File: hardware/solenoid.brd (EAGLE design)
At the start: 37.3 x 34 mm, 32 parts, among them U2 AP2204R

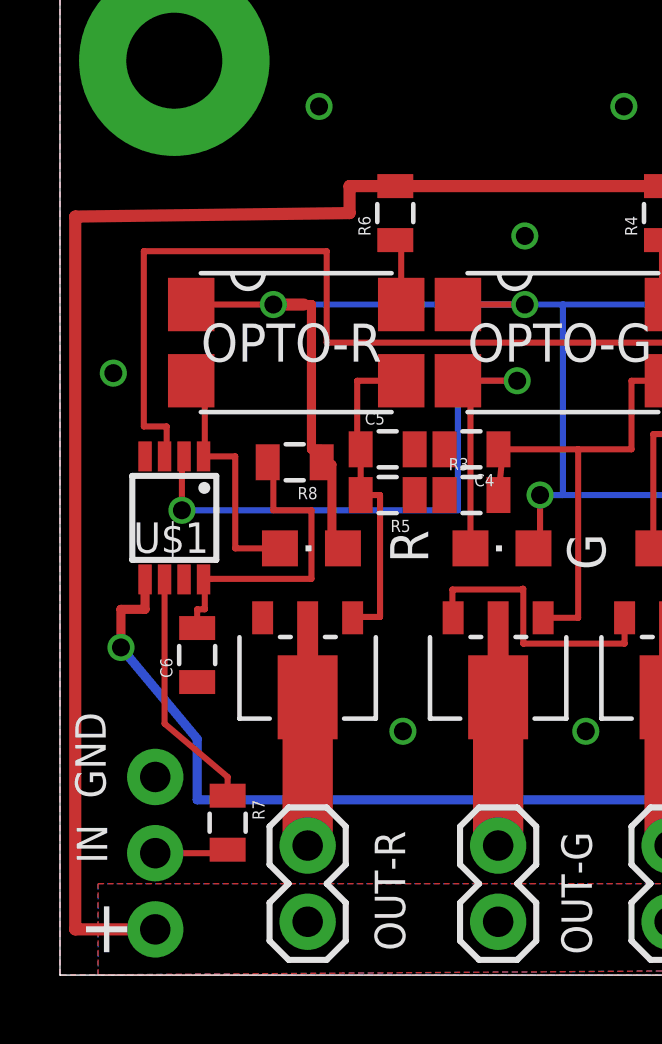
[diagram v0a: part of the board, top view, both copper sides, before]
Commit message: Fixed GND via(s) name
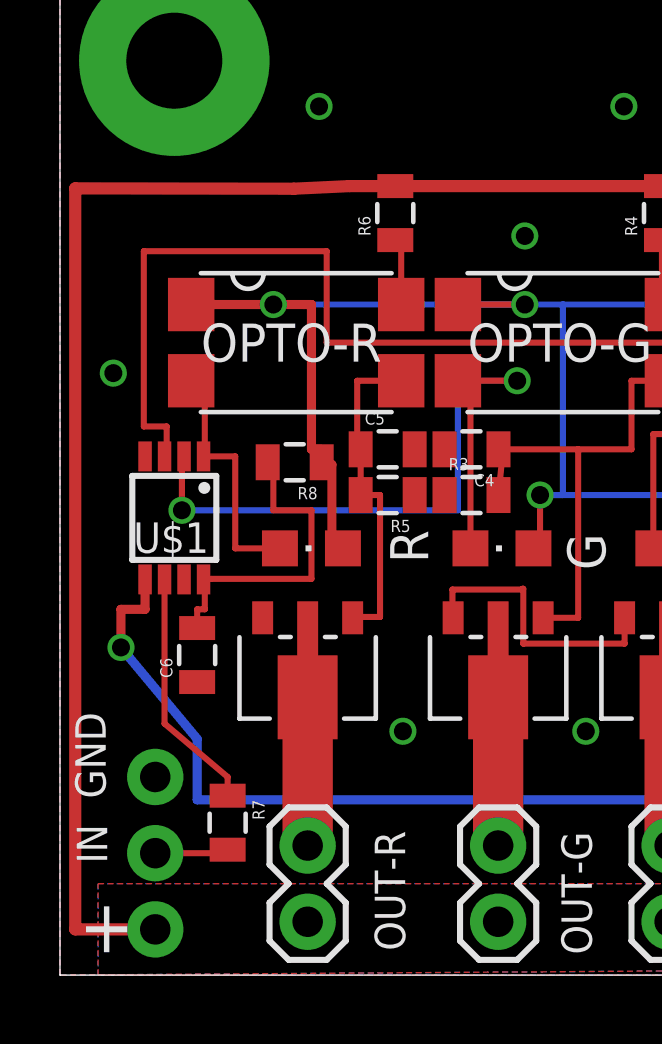
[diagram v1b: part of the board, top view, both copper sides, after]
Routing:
- net GND: vias 0 -> 12
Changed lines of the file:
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@@
 <wire x1="15.4432" y1="11.049" x2="18.82" y2="11.049" width="0.2032" layer="1"/>
 <wire x1="18.82" y1="11.049" x2="18.82" y2="11.91" width="0.2032" layer="1"/>
+<via x="1.778" y="20.066" extent="1-16" drill="0.6"/>
+<via x="11.43" y="8.128" extent="1-16" drill="0.6"/>
+<via x="17.526" y="8.128" extent="1-16" drill="0.6"/>
+<via x="35.306" y="2.032" extent="1-16" drill="0.6"/>
+<via x="27.94" y="12.446" extent="1-16" drill="0.6"/>
+<via x="27.686" y="16.764" extent="1-16" drill="0.6"/>
+<via x="35.052" y="27.432" extent="1-16" drill="0.6"/>
+<via x="24.892" y="28.194" extent="1-16" drill="0.6"/>
+<via x="24.892" y="25.146" extent="1-16" drill="0.6"/>
+<via x="15.494" y="24.638" extent="1-16" drill="0.6"/>
+<via x="18.796" y="28.956" extent="1-16" drill="0.6"/>
+<via x="8.636" y="28.956" extent="1-16" drill="0.6"/>
 </signal>
 <signal name="VDD">
@@
 <wire x1="29.464" y1="26.3" x2="29.464" y2="26.046" width="0.4064" layer="1"/>
 <wire x1="11.176" y1="26.3" x2="9.652" y2="26.3" width="0.4064" layer="1"/>
-<wire x1="9.652" y1="26.3" x2="9.652" y2="25.4" width="0.4064" layer="1"/>
-<wire x1="9.652" y1="25.4" x2="0.508" y2="25.284" width="0.4064" layer="1"/>
-<wire x1="0.508" y1="25.284" x2="0.508" y2="1.524" width="0.4064" layer="1"/>
+<wire x1="9.652" y1="26.3" x2="7.7978" y2="26.2128" width="0.4064" layer="1"/>
+<wire x1="7.7978" y1="26.2128" x2="0.508" y2="26.2238" width="0.4064" layer="1"/>
+<wire x1="0.508" y1="26.2238" x2="0.508" y2="1.524" width="0.4064" layer="1"/>
 <wire x1="0.508" y1="1.524" x2="3.175" y2="1.524" width="0.4064" layer="1"/>
 <polygon width="0.4064" layer="16" thermals="no">
@@
 <wire x1="33.782" y1="9.398" x2="32.142" y2="9.398" width="0.4064" layer="1"/>
 <wire x1="32.142" y1="9.398" x2="32.142" y2="9.144" width="0.4064" layer="1"/>
-<wire x1="7.112" y1="22.352" x2="4.374" y2="22.352" width="0.2032" layer="1"/>
+<wire x1="7.112" y1="22.352" x2="4.374" y2="22.352" width="0.3048" layer="1"/>
 <via x="7.112" y="22.352" extent="1-16" drill="0.6"/>
 <wire x1="7.112" y1="22.352" x2="15.494" y2="22.352" width="0.2032" layer="16"/>
@@
 <wire x1="16.764" y1="22.352" x2="24.638" y2="22.352" width="0.2032" layer="16"/>
 <wire x1="16.764" y1="22.352" x2="15.494" y2="22.352" width="0.2032" layer="16"/>
-<wire x1="7.112" y1="22.352" x2="8.128" y2="22.352" width="0.4064" layer="1"/>
+<wire x1="7.112" y1="22.352" x2="8.128" y2="22.352" width="0.3048" layer="1"/>
 <wire x1="15.782" y1="14.224" x2="16.002" y2="14.224" width="0.2032" layer="1"/>
 <wire x1="16.002" y1="14.224" x2="16.002" y2="16.002" width="0.2032" layer="1"/>
@@
 <wire x1="4.572" y1="7.874" x2="2.032" y2="10.922" width="0.3048" layer="16"/>
 </signal>
-<signal name="N$15">
-<via x="8.636" y="28.956" extent="1-16" drill="0.6"/>
-</signal>
-<signal name="N$16">
-<via x="35.052" y="27.432" extent="1-16" drill="0.6"/>
-</signal>
-<signal name="N$17">
-<via x="18.796" y="28.956" extent="1-16" drill="0.6"/>
-</signal>
-<signal name="N$18">
-<via x="15.494" y="24.638" extent="1-16" drill="0.6"/>
-</signal>
-<signal name="N$19">
-<via x="24.892" y="25.146" extent="1-16" drill="0.6"/>
-</signal>
-<signal name="N$20">
-<via x="27.686" y="16.764" extent="1-16" drill="0.6"/>
-</signal>
-<signal name="N$21">
-<via x="35.306" y="2.032" extent="1-16" drill="0.6"/>
-</signal>
-<signal name="N$23">
-<via x="27.94" y="12.446" extent="1-16" drill="0.6"/>
-</signal>
-<signal name="N$26">
-<via x="1.778" y="20.066" extent="1-16" drill="0.6"/>
-</signal>
-<signal name="N$27">
-<via x="17.526" y="8.128" extent="1-16" drill="0.6"/>
-</signal>
-<signal name="N$28">
-<via x="11.43" y="8.128" extent="1-16" drill="0.6"/>
-</signal>
-<signal name="N$29">
-<via x="24.892" y="28.194" extent="1-16" drill="0.6"/>
-</signal>
 <signal name="N$30">

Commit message: Put in values for the low pass resistors and caps, This is an estimate.
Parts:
- C3, C4, C5: value (none) -> 400nf
- R1, R3, R5: value (none) -> 1000
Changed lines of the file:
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@@
 <attribute name="OC_NEWARK" value="unknown" x="25.654" y="21.082" size="1.778" layer="27" rot="R270" display="off"/>
 </element>
-<element name="R1" library="SparkFun-Passives" package="0805" value="" x="25.019" y="11.938" rot="R180"/>
+<element name="R1" library="SparkFun-Passives" package="0805" value="1000" x="25.019" y="11.938" rot="R180"/>
 <element name="R2" library="SparkFun-Passives" package="0805" value="220" x="29.464" y="25.146" rot="R90"/>
 <element name="U$1" library="mishafarms" package="MSOP8" value="WS2811S" x="3.81" y="15.24" smashed="yes" rot="R180">
@@
 </element>
 <element name="C2" library="SparkFun-Capacitors" package="0805" value="2.2uf" x="31.242" y="9.144" rot="R180"/>
-<element name="C3" library="SparkFun-Capacitors" package="0805" value="" x="25.019" y="13.843"/>
+<element name="C3" library="SparkFun-Capacitors" package="0805" value="400nf" x="25.019" y="13.843"/>
 <element name="$T2" library="mishafarms" package="SOT89R" value="BSS606N" x="14.605" y="10.16" smashed="yes" rot="R180"/>
 <element name="OPTO-G" library="optocoupler" package="SMD4" value="LTV816S" x="16.764" y="21.082" smashed="yes" rot="R270">
@@
 <attribute name="OC_NEWARK" value="unknown" x="39.624" y="31.242" size="1.778" layer="27" rot="R270" display="off"/>
 </element>
-<element name="R3" library="SparkFun-Passives" package="0805" value="" x="13.716" y="16.002"/>
+<element name="R3" library="SparkFun-Passives" package="0805" value="1000" x="13.716" y="16.002"/>
 <element name="R4" library="SparkFun-Passives" package="0805" value="220" x="20.066" y="25.4" rot="R90"/>
 <element name="G" library="led" package="CHIPLED_0805" value="" x="14.732" y="14.224" smashed="yes" rot="R90">
@@
 <attribute name="VALUE" x="17.78" y="0.508" size="1.27" layer="27" rot="R90"/>
 </element>
-<element name="C4" library="SparkFun-Capacitors" package="0805" value="" x="13.716" y="17.526" rot="R180"/>
+<element name="C4" library="SparkFun-Capacitors" package="0805" value="400nf" x="13.716" y="17.526" rot="R180"/>
 <element name="$T3" library="mishafarms" package="SOT89R" value="BSS606N" x="8.255" y="10.16" smashed="yes" rot="R180"/>
 <element name="OPTO-R" library="optocoupler" package="SMD4" value="LTV816S" x="7.874" y="21.082" smashed="yes" rot="R270">
@@
 <attribute name="OC_NEWARK" value="unknown" x="30.734" y="31.242" size="1.778" layer="27" rot="R270" display="off"/>
 </element>
-<element name="R5" library="SparkFun-Passives" package="0805" value="" x="10.922" y="16.002" rot="R180"/>
+<element name="R5" library="SparkFun-Passives" package="0805" value="1000" x="10.922" y="16.002" rot="R180"/>
 <element name="R6" library="SparkFun-Passives" package="0805" value="220" x="11.176" y="25.4" rot="R90"/>
 <element name="R" library="led" package="CHIPLED_0805" value="" x="8.382" y="14.224" smashed="yes" rot="R90">
@@
 <attribute name="VALUE" x="11.43" y="0.508" size="1.27" layer="27" rot="R90"/>
 </element>
-<element name="C5" library="SparkFun-Capacitors" package="0805" value="" x="10.922" y="17.526"/>
+<element name="C5" library="SparkFun-Capacitors" package="0805" value="400nf" x="10.922" y="17.526"/>
 <element name="IN" library="SparkFun-Connectors" package="1X03_NO_SILK" value="" x="3.175" y="6.604" smashed="yes" rot="R270">
 <attribute name="NAME" x="0.5588" y="5.0292" size="1.016" layer="21" font="vector" ratio="10" rot="R270"/>

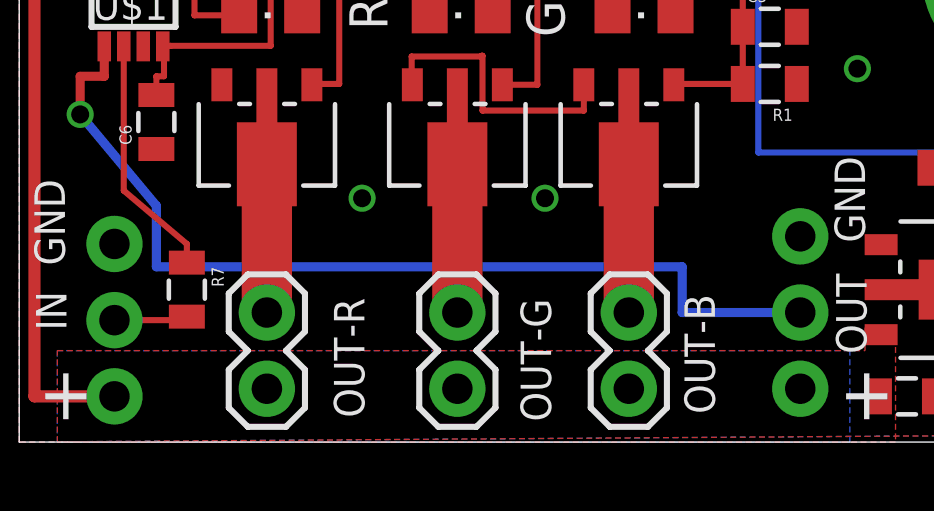
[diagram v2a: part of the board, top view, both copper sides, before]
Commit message: Added protection diodes
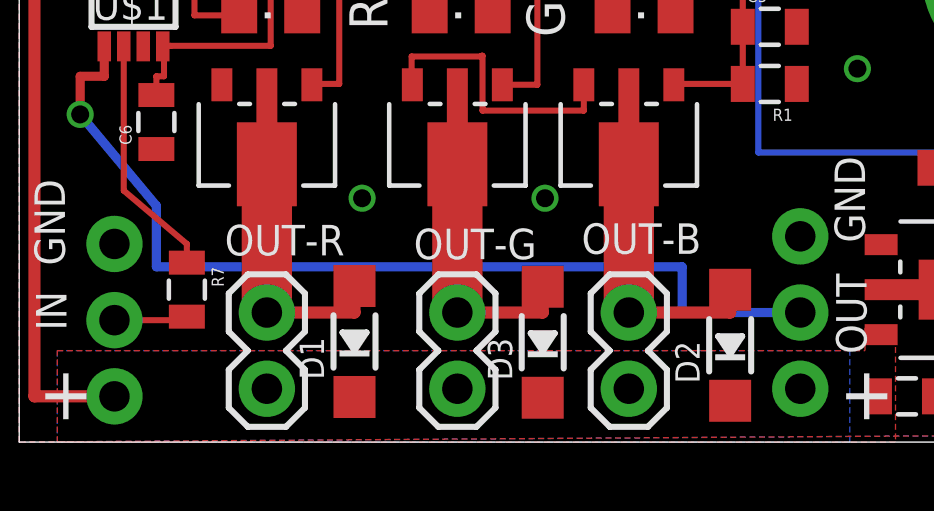
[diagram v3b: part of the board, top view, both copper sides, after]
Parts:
- added D1, D2, D3: (no value), microbuilder:SOD-123
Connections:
- net N$12: now also D1.A
- net N$4: now also D2.A
- net N$8: now also D3.A
- net VDD: now also D1.C, D2.C, D3.C
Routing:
- net N$4: track 7.24 -> 11.4 mm
- net N$12: track 7.24 -> 11.0 mm
- net N$8: track 7.24 -> 10.9 mm
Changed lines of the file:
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@@
 <element name="$T1" library="mishafarms" package="SOT89R" value="BSS606N" x="20.32" y="10.16" smashed="yes" rot="R180"/>
 <element name="OUT-B" library="SparkFun-Connectors" package="1X02" value="" x="20.32" y="1.778" smashed="yes" rot="R90">
-<attribute name="NAME" x="23.1902" y="0.9398" size="1.016" layer="21" font="vector" ratio="10" rot="R90"/>
+<attribute name="NAME" x="18.7452" y="6.2738" size="1.016" layer="21" font="vector" ratio="10"/>
 <attribute name="VALUE" x="23.495" y="0.508" size="1.27" layer="27" rot="R90"/>
 </element>
@@
 </element>
 <element name="OUT-G" library="SparkFun-Connectors" package="1X02" value="" x="14.605" y="1.778" smashed="yes" rot="R90">
-<attribute name="NAME" x="17.7292" y="0.6858" size="1.016" layer="21" font="vector" ratio="10" rot="R90"/>
+<attribute name="NAME" x="17.2466" y="7.112" size="1.016" layer="21" font="vector" ratio="10" rot="R180"/>
 <attribute name="VALUE" x="17.78" y="0.508" size="1.27" layer="27" rot="R90"/>
 </element>
@@
 </element>
 <element name="OUT-R" library="SparkFun-Connectors" package="1X02" value="" x="8.255" y="1.778" smashed="yes" rot="R90">
-<attribute name="NAME" x="11.5062" y="0.8128" size="1.016" layer="21" font="vector" ratio="10" rot="R90"/>
+<attribute name="NAME" x="10.8458" y="7.239" size="1.016" layer="21" font="vector" ratio="10" rot="R180"/>
 <attribute name="VALUE" x="11.43" y="0.508" size="1.27" layer="27" rot="R90"/>
 </element>
@@
 <element name="C6" library="SparkFun-Capacitors" package="0805" value=".1uf" x="4.572" y="10.668" rot="R90"/>
 <element name="R8" library="SparkFun-Passives" package="0805" value="100" x="7.8232" y="17.0942" rot="R180"/>
+<element name="D1" library="microbuilder" package="SOD-123" value="" x="11.176" y="3.3528" rot="R90"/>
+<element name="D2" library="microbuilder" package="SOD-123" value="" x="23.6982" y="3.2258" rot="R90"/>
+<element name="D3" library="microbuilder" package="SOD-123" value="" x="17.4498" y="3.3274" rot="R90"/>
 </elements>
 <signals>
@@
 <vertex x="27.686" y="3.048"/>
 </polygon>
+<contactref element="D1" pad="C"/>
+<contactref element="D2" pad="C"/>
+<contactref element="D3" pad="C"/>
 </signal>
 <signal name="VCC">
@@
 <wire x1="20.32" y1="9.26" x2="20.32" y2="4.318" width="1.6764" layer="1"/>
 <wire x1="20.32" y1="11.56" x2="20.32" y2="9.26" width="0.4064" layer="1"/>
+<contactref element="D2" pad="A"/>
+<wire x1="20.32" y1="4.318" x2="23.6982" y2="4.318" width="0.4064" layer="1"/>
+<wire x1="23.6982" y1="4.318" x2="23.6982" y2="5.0758" width="0.4064" layer="1"/>
 </signal>
 <signal name="N$5">
@@
 <wire x1="14.605" y1="9.26" x2="14.605" y2="4.318" width="1.6764" layer="1"/>
 <wire x1="14.605" y1="11.56" x2="14.605" y2="9.26" width="0.4064" layer="1"/>
+<contactref element="D3" pad="A"/>
+<wire x1="14.605" y1="4.318" x2="17.4498" y2="4.318" width="0.4064" layer="1"/>
+<wire x1="17.4498" y1="4.318" x2="17.4498" y2="5.1774" width="0.4064" layer="1"/>
 </signal>
 <signal name="N$9">
@@
 <wire x1="8.255" y1="9.26" x2="8.255" y2="4.318" width="1.6764" layer="1"/>
 <wire x1="8.255" y1="11.56" x2="8.255" y2="9.26" width="0.4064" layer="1"/>
+<contactref element="D1" pad="A"/>
+<wire x1="8.255" y1="4.318" x2="11.176" y2="4.318" width="0.4064" layer="1"/>
+<wire x1="11.176" y1="4.318" x2="11.176" y2="5.2028" width="0.4064" layer="1"/>
 </signal>
 <signal name="N$13">
